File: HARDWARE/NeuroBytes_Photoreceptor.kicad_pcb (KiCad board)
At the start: 2 copper layers, 46.8 x 19.8 mm, 24 parts, among them P1 JST_GH_4-POS, P2 JST_GH_4-POS, P3 JST_GH_7-POS, SW1 SW_PB_4term, SW2 SW_PB_4term, U1 APDS9007, U2 STM32L011Gx, U3 LD3985M33R

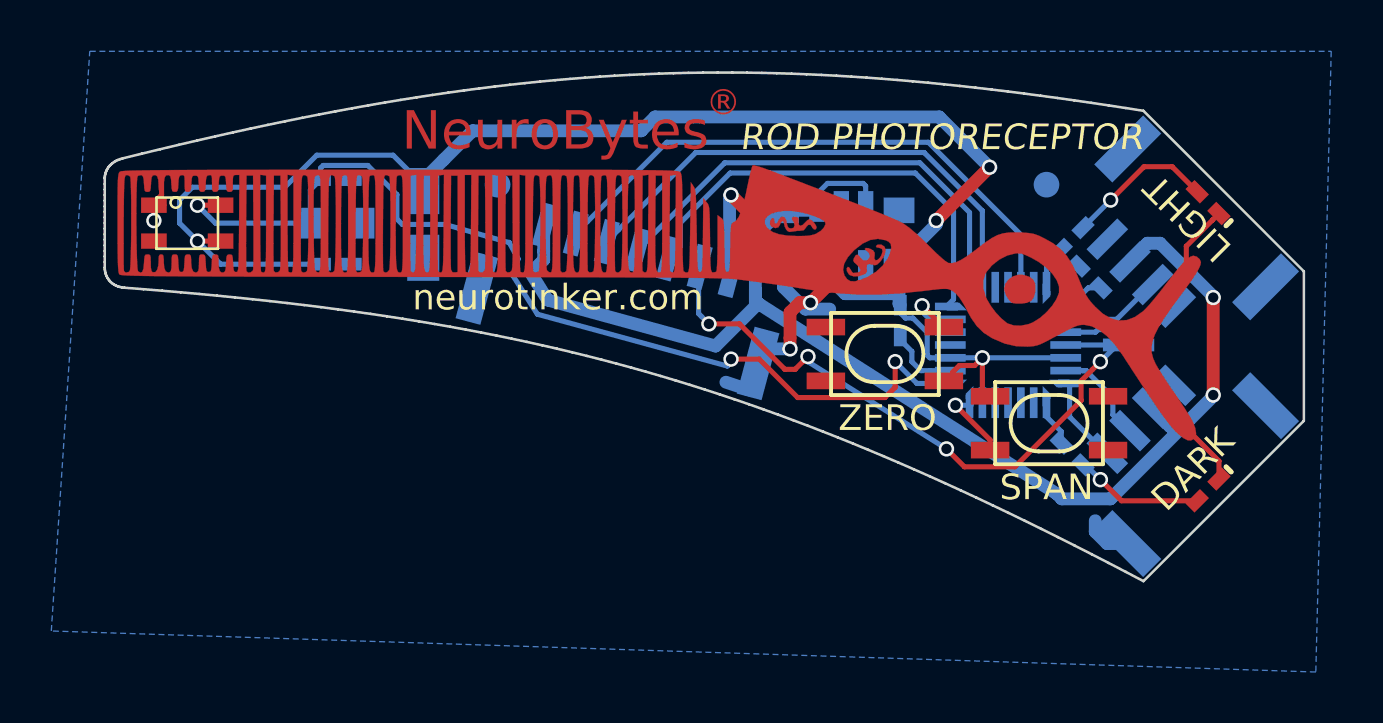
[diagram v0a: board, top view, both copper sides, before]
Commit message: Changed to 5-pin JST GH connector for programming and power. Added POWER label. Minor routing changes.
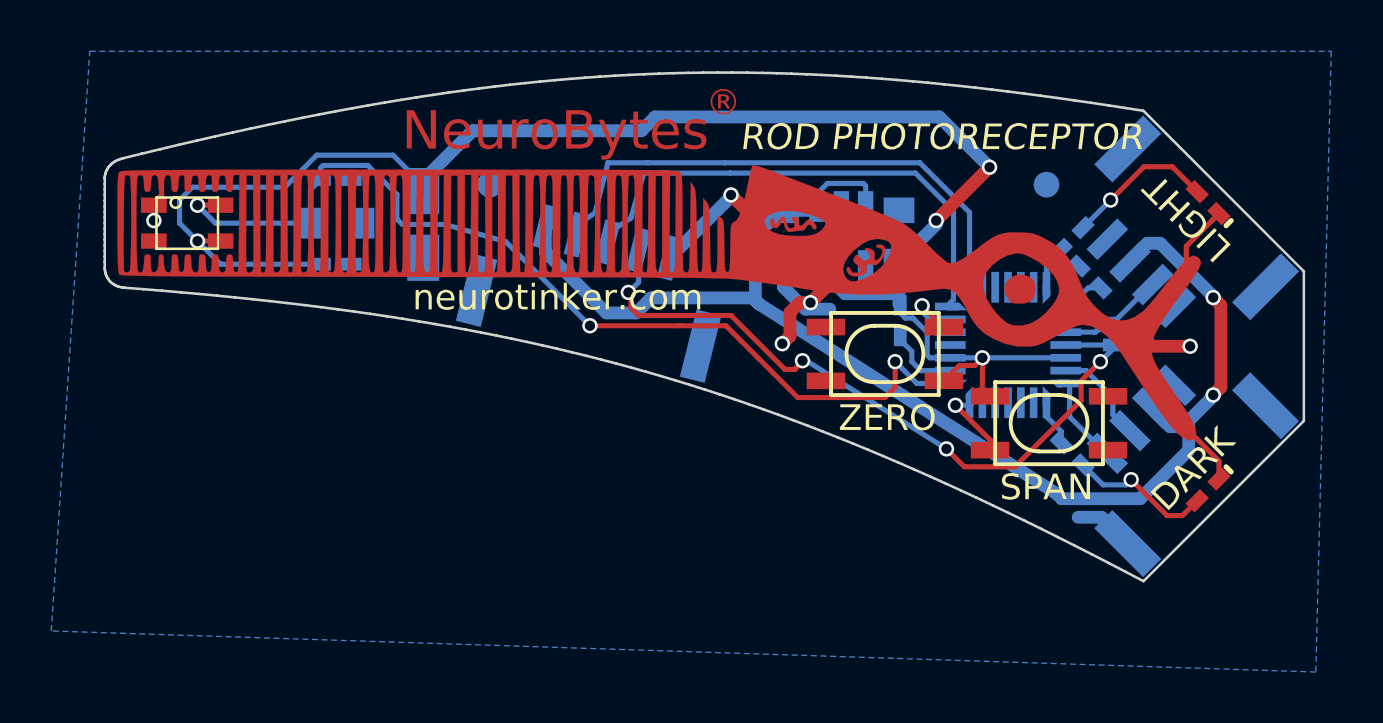
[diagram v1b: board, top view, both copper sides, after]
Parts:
- P3: value JST_GH_7-POS -> JST_GH_5-pos; footprint KiCad_Footprints:ZF_CONN_JST_GH_7POS -> KiCad_Footprints:ZF_CONN_JST_GH_5POS
- moved P3 1.19 mm to (184.0, 98.3), turned to 256 degrees
- moved REF** 0.30 mm to (179.8, 94.5)
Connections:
- net SWCLK/MISO renamed SWCLK
- net SWDIO/SCK renamed SWDIO
- P3 pad 5: NSS -> +5V
- U2 pad 23: NSS -> Net-(U2-Pad23)
- U2 pad 26: MOSI -> Net-(U2-Pad26)
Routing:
- net MOSI: track 22.4 -> 0.00 mm
- net NSS: track 20.1 -> 0.00 mm
- net SWCLK: track 18.4 -> 21.6 mm
- net RESET: track 25.3 -> 28.1 mm
- net SWDIO: track 17.5 -> 19.8 mm
- net +5V: track 53.8 -> 52.3 mm
- net GND: track 55.9 -> 54.8 mm, vias 4 -> 5
- net Net-(D2-Pad2): track 5.03 -> 5.78 mm
- net SENSE: track 39.2 -> 38.6 mm
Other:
- board text added: "POWER"

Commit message: updated component descriptions. reloaded netlist. minor PCB updates. fresh *.csv export.
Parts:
- C3, C4, C5: value 1 uF -> 1u
- U3: value LD3985M33R -> 3v3 LDO
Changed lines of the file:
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@@
-(kicad_pcb (version 4) (host pcbnew 4.0.5-e0-6337~49~ubuntu14.04.1)
+(kicad_pcb (version 4) (host pcbnew 4.0.7-e1-6374~58~ubuntu14.04.1)
   (general
-    (links 0)
-    (no_connects 0)
-    (area 164.733488 90.077587 211.583735 110.008306)
+    (links 62)
+    (no_connects 1)
+    (area 152 73.8 248.857146 152.55)
     (thickness 1.6)
     (drawings 220)
@@
     (mod_text_size 1 1)
     (mod_text_width 0.15)
-    (pad_size 1 1)
+    (pad_size 1 2.7)
     (pad_drill 0)
     (pad_to_mask_clearance 0)
@@
     (visible_elements FFFFFF7F)
     (pcbplotparams
-      (layerselection 0x00020_00000000)
+      (layerselection 0x200fc_80000001)
       (usegerberextensions false)
       (excludeedgelayer true)
@@
       (drillshape 0)
       (scaleselection 1)
-      (outputdirectory NeuroTinker_NeuroBytes_Photoreceptor_RFQ_05312017_Macrofab/))
+      (outputdirectory ../../../NeuroTinker_RFQ_Sept2017/NeuroBytes_Photoreceptor/))
   )
   (net 0 "")
@@
       (effects (font (size 1 1) (thickness 0.15)) (justify mirror))
     )
-    (fp_text value "1 uF" (at 0 4.7) (layer B.Fab) hide
+    (fp_text value 1u (at 0 4.7) (layer B.Fab) hide
       (effects (font (size 1 1) (thickness 0.15)) (justify mirror))
     )
@@
       (effects (font (size 1 1) (thickness 0.15)) (justify mirror))
     )
-    (fp_text value "1 uF" (at 0 4.7 270) (layer B.Fab) hide
+    (fp_text value 1u (at 0 4.7 270) (layer B.Fab) hide
       (effects (font (size 1 1) (thickness 0.15)) (justify mirror))
     )
@@
       (effects (font (size 1 1) (thickness 0.15)) (justify mirror))
     )
-    (fp_text value LD3985M33R (at 0 3.5) (layer B.Fab) hide
+    (fp_text value "3v3 LDO" (at 0 3.5) (layer B.Fab) hide
       (effects (font (size 1 1) (thickness 0.15)) (justify mirror))
     )
@@
       (effects (font (size 1 1) (thickness 0.15)) (justify mirror))
     )
-    (fp_text value "1 uF" (at 0 4.7 90) (layer B.Fab) hide
+    (fp_text value 1u (at 0 4.7 90) (layer B.Fab) hide
       (effects (font (size 1 1) (thickness 0.15)) (justify mirror))
     )
@@
   (module KiCad_Footprints:ZF_SW_PTS810 (layer F.Cu)
     (at 195.2 101.1 270)
+    (attr smd)
     (fp_text reference SW1 (at 0 3.6 270) (layer F.Fab)
       (effects (font (size 1 1) (thickness 0.15)))
@@
   (module KiCad_Footprints:ZF_SW_PTS810 (layer F.Cu)
     (at 201.6 103.8 90)
+    (attr smd)
     (fp_text reference SW2 (at 0 3.6 90) (layer F.Fab)
       (effects (font (size 1 1) (thickness 0.15)))
